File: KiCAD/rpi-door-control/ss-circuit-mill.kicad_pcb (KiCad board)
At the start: 2 copper layers, 103.5 x 49.5 mm, 26 parts, among them IC1 4N35, J1 RJ45, P1 CONN_13X2, P2 CONN_2, P3 CONN_2, P4 CONN_2, Q1 2N3904, Q2 2N3904, SW1 SW_PUSH, U1 RELAY

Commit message: 12V circuit is done but man the data side is tricky
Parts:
- P2: value CONN_2 -> LOCK BTN
- P3: value CONN_2 -> MAGLOCK
- P4: value CONN_2 -> +12V
- moved D4 67.1 mm to (179.7, 69.5)
- moved P1 57.4 mm to (96.2, 103.7), turned to 270 degrees
- moved SW1 48.1 mm to (100.2, 72.5), turned to 180 degrees
- moved J1 37.5 mm to (128.1, 70.3), turned to 180 degrees
- moved P2 34.0 mm to (112.0, 73.7), turned to 0 degrees
- moved U1 31.6 mm to (156.2, 85.0), turned to 90 degrees
- moved P4 24.1 mm to (178.4, 82.5)
- moved Q2 22.9 mm to (167.2, 101.2), turned to 0 degrees
- moved D5 21.7 mm to (159.5, 100.1), turned to 90 degrees
- moved R6 21.7 mm to (132.6, 104.5), turned to 90 degrees
- moved R12 19.2 mm to (168.3, 78.7)
- moved R1 18.9 mm to (102.2, 83.4), turned to 180 degrees
- moved P3 18.9 mm to (178.5, 100.5)
- moved R7 9.47 mm to (152.8, 99.5), turned to 270 degrees
- moved R11 6.38 mm to (136.9, 89.8)
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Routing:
- net /BELL: track 0.00 -> 67.2 mm
- net +5V: track 0.00 -> 59.6 mm
- net +12V: track 0.00 -> 54.8 mm
- net /GPIO17: track 0.00 -> 49.3 mm
- net GNDPWR: track 0.00 -> 48.7 mm
- net N-0000037: track 0.00 -> 45.8 mm
- net N-0000021: track 0.00 -> 28.3 mm
- net N-0000026: track 0.00 -> 27.9 mm
- net N-0000022: track 0.00 -> 13.0 mm
- net N-000006: track 0.00 -> 9.85 mm
- net +3.3V: track 0.00 -> 5.42 mm
- added copper zone on B.Cu, net (none)
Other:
- board size 103.5 x 49.5 mm -> 133.5 x 88.5 mm
- net class 12V POWER: clearance 2 -> 0.5; trace_width 3 -> 2
- net class Default: clearance 1 -> 0.5
- rule trace_clearance: 1 -> 0.5

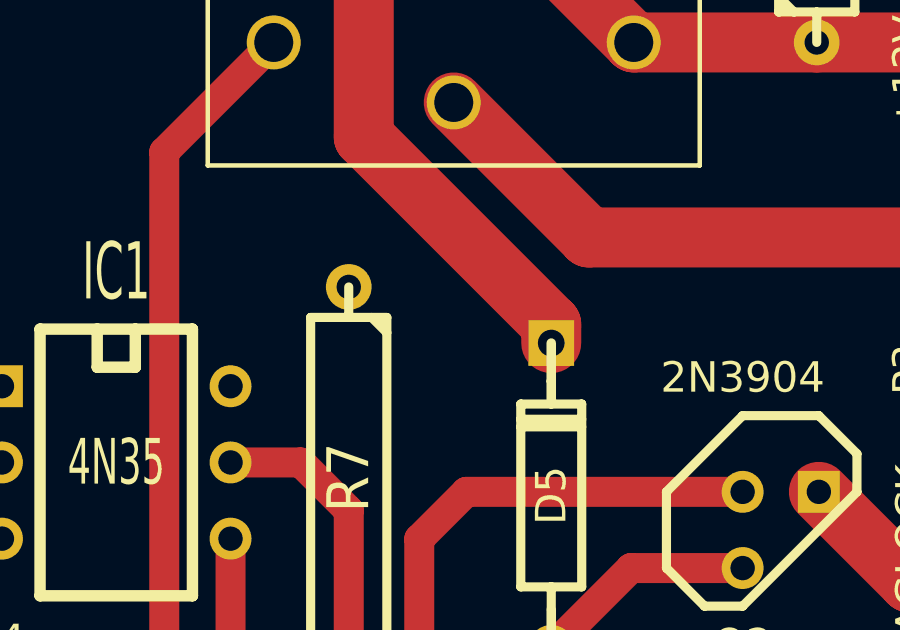
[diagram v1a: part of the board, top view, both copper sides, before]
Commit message: Missed a track on the power side
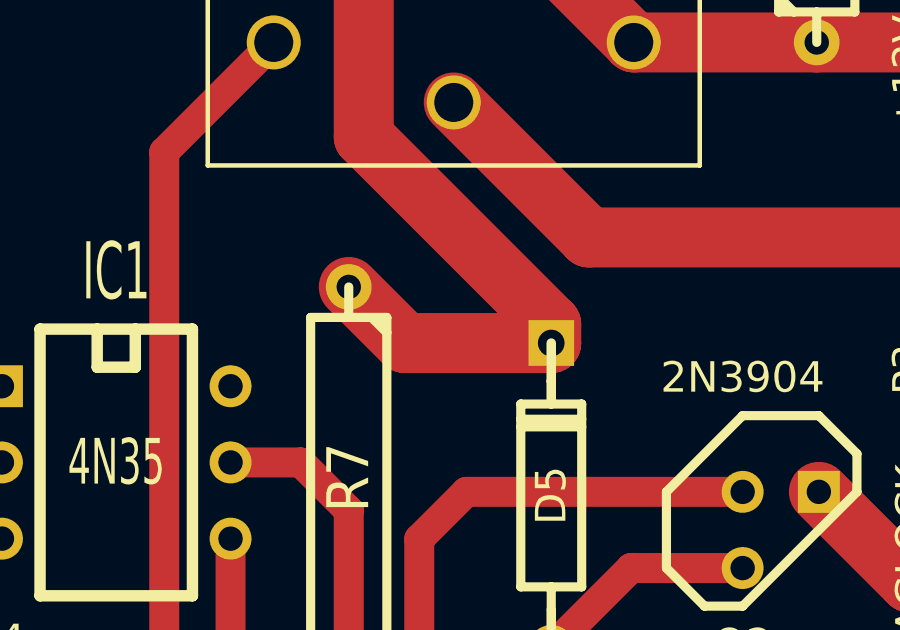
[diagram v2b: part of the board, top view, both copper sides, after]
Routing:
- net +12V: track 54.8 -> 62.3 mm
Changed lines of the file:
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@@
   (general
     (links 48)
-    (no_connects 26)
-    (area 0 0 0 0)
+    (no_connects 25)
+    (area 71.424999 52.924999 205.075001 141.575001)
     (thickness 1.6)
     (drawings 4)
-    (tracks 67)
+    (tracks 69)
     (zones 0)
     (modules 26)
@@
   (gr_line (start 205 53) (end 205 141.5) (angle 90) (layer Edge.Cuts) (width 0.15))
   (gr_line (start 71.5 53) (end 205 53) (angle 90) (layer Edge.Cuts) (width 0.15))
+  (segment (start 159.5 95.02) (end 154.62 95.02) (width 2) (layer F.Cu) (net 1) (status 400000))
+  (segment (start 154.62 95.02) (end 152.75 93.15) (width 2) (layer F.Cu) (net 1) (status 800000))
   (segment (start 159.5 95.02) (end 159.5 94.4) (width 2) (layer F.Cu) (net 1))
   (segment (start 153.25 76.5) (end 153.5 76.25) (width 2) (layer F.Cu) (net 1))
@@
   (segment (start 150.25 73) (end 153.5 76.25) (width 2) (layer F.Cu) (net 1))
   (segment (start 153.5 76.25) (end 162.25 85) (width 2) (layer F.Cu) (net 1))
-  (segment (start 94.93 88.46) (end 94.93 84.27) (width 1) (layer F.Cu) (net 2) (status 400000))
-  (segment (start 94.93 84.27) (end 95.8 83.4) (width 1) (layer F.Cu) (net 2) (status 800000))
-  (segment (start 136.9 83.45) (end 136.9 76.95) (width 1) (layer F.Cu) (net 3) (status 400000))
-  (segment (start 129.865 74.25) (end 127.465 76.65) (width 1) (layer F.Cu) (net 3) (status 800000))
+  (segment (start 94.93 88.46) (end 94.93 84.27) (width 1) (layer F.Cu) (net 2))
+  (segment (start 94.93 84.27) (end 95.8 83.4) (width 1) (layer F.Cu) (net 2))
+  (segment (start 136.9 83.45) (end 136.9 76.95) (width 1) (layer F.Cu) (net 3))
+  (segment (start 129.865 74.25) (end 127.465 76.65) (width 1) (layer F.Cu) (net 3))
   (segment (start 134.2 74.25) (end 129.865 74.25) (width 1) (layer F.Cu) (net 3))
   (segment (start 136.9 76.95) (end 134.2 74.25) (width 1) (layer F.Cu) (net 3))
-  (segment (start 97.47 88.46) (end 106.94 88.46) (width 1) (layer F.Cu) (net 3) (status 400000))
-  (segment (start 111.95 83.45) (end 136.9 83.45) (width 1) (layer F.Cu) (net 3) (status 800000))
+  (segment (start 97.47 88.46) (end 106.94 88.46) (width 1) (layer F.Cu) (net 3))
+  (segment (start 111.95 83.45) (end 136.9 83.45) (width 1) (layer F.Cu) (net 3))
   (segment (start 106.94 88.46) (end 111.95 83.45) (width 1) (layer F.Cu) (net 3))
-  (segment (start 94.93 103.7) (end 94.4 103.7) (width 1) (layer F.Cu) (net 4) (status C00000))
-  (segment (start 120.55 76.65) (end 124.925 76.65) (width 1) (layer F.Cu) (net 4) (status 800000))
+  (segment (start 94.93 103.7) (end 94.4 103.7) (width 1) (layer F.Cu) (net 4))
+  (segment (start 120.55 76.65) (end 124.925 76.65) (width 1) (layer F.Cu) (net 4))
   (segment (start 115.2 71.3) (end 120.55 76.65) (width 1) (layer F.Cu) (net 4))
   (segment (start 108.75 71.3) (end 115.2 71.3) (width 1) (layer F.Cu) (net 4))
@@
   (segment (start 91.05 76.75) (end 95.15 72.65) (width 1) (layer F.Cu) (net 4))
   (segment (start 91.05 100.35) (end 91.05 76.75) (width 1) (layer F.Cu) (net 4))
-  (segment (start 94.4 103.7) (end 91.05 100.35) (width 1) (layer F.Cu) (net 4) (status 400000))
-  (segment (start 109.45 73.7) (end 109.45 82.45) (width 1) (layer F.Cu) (net 5) (status 400000))
-  (segment (start 109.45 82.45) (end 108.5 83.4) (width 1) (layer F.Cu) (net 5) (status 800000))
-  (segment (start 103.96 75.09) (end 103.96 78.86) (width 1) (layer F.Cu) (net 5) (status 400000))
-  (segment (start 103.96 78.86) (end 108.5 83.4) (width 1) (layer F.Cu) (net 5) (status 800000))
+  (segment (start 94.4 103.7) (end 91.05 100.35) (width 1) (layer F.Cu) (net 4))
+  (segment (start 109.45 73.7) (end 109.45 82.45) (width 1) (layer F.Cu) (net 5))
+  (segment (start 109.45 82.45) (end 108.5 83.4) (width 1) (layer F.Cu) (net 5))
+  (segment (start 103.96 75.09) (end 103.96 78.86) (width 1) (layer F.Cu) (net 5))
+  (segment (start 103.96 78.86) (end 108.5 83.4) (width 1) (layer F.Cu) (net 5))
   (segment (start 94.93 101.16) (end 94.11 101.16) (width 1) (layer F.Cu) (net 5))
   (segment (start 92.6 78.83) (end 96.34 75.09) (width 1) (layer F.Cu) (net 5))

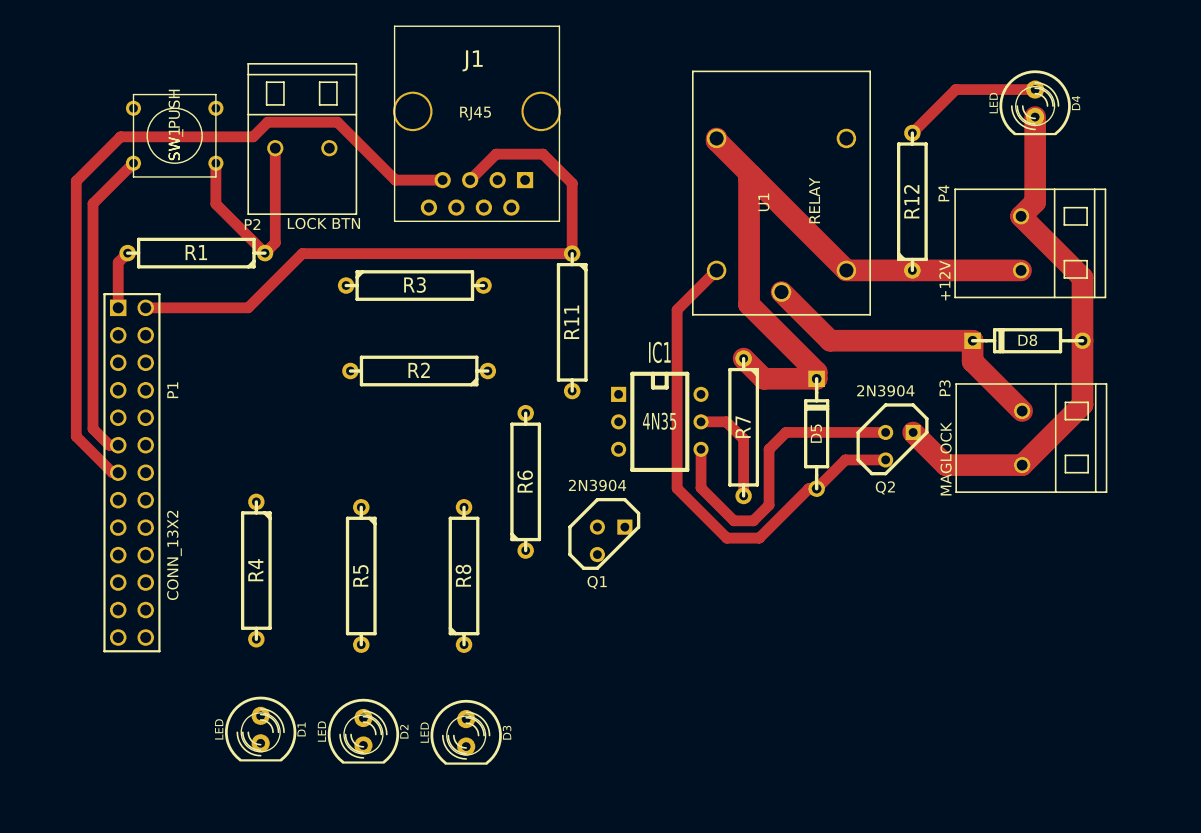
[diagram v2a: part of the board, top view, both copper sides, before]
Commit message: drew up single sided board but can't connect grounds.  Needs serious rerouting
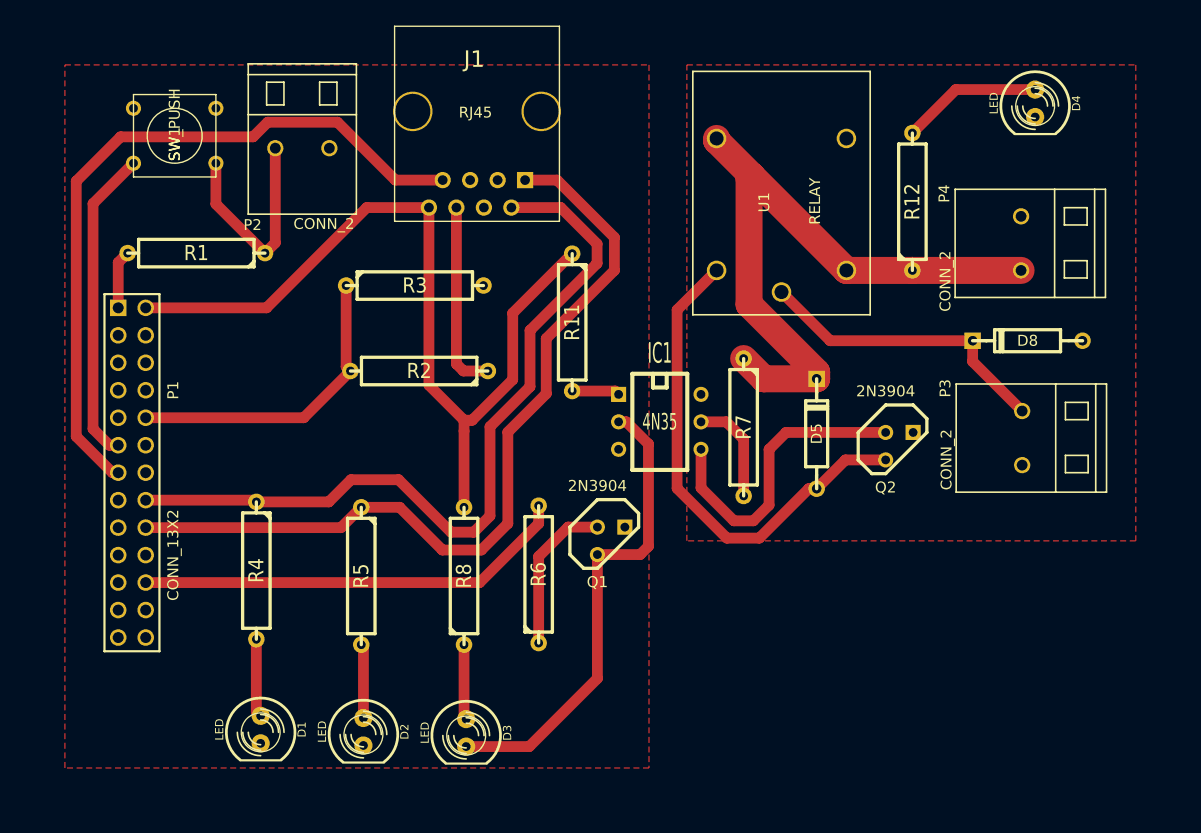
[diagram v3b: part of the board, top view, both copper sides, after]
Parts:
- P2: value LOCK BTN -> CONN_2
- P3: value MAGLOCK -> CONN_2
- P4: value +12V -> CONN_2
- moved R6 8.63 mm to (133.8, 113.1)
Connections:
- J1 pad 5: +5V -> (no net)
- J1 pad 8: (no net) -> +5V
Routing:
- net /GPIO24: track 0.00 -> 77.9 mm
- net /GPIO23: track 0.00 -> 73.9 mm
- net GNDPWR: track 48.7 -> 0.00 mm
- net N-0000025: track 0.00 -> 44.3 mm
- net /GPIO25: track 0.00 -> 40.2 mm
- net /RXD: track 0.00 -> 28.8 mm
- net +5V: track 59.6 -> 79.1 mm
- net /RFID TXD: track 0.00 -> 17.6 mm
- net N-000003: track 0.00 -> 14.6 mm
- net N-000002: track 0.00 -> 7.25 mm
- net N-0000026: track 0.00 -> 6.96 mm
- net N-000001: track 0.00 -> 6.86 mm
- net N-0000019: track 0.00 -> 4.42 mm
- added copper zone on F.Cu, net GND
- added copper zone on F.Cu, net GNDPWR
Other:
- net class 12V POWER: trace_width 2 -> 2.5

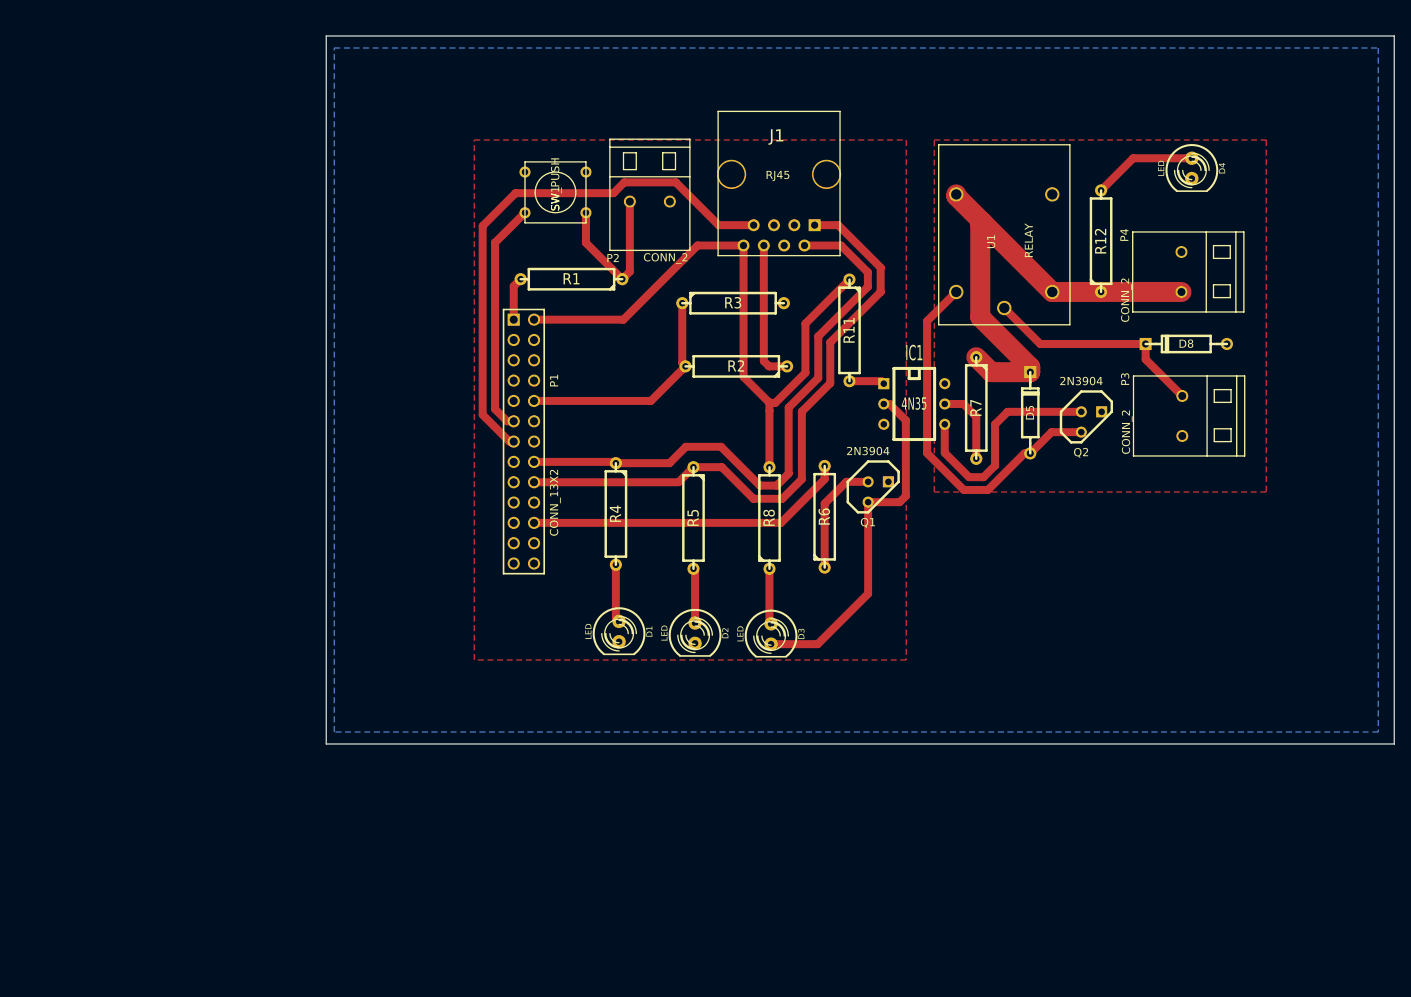
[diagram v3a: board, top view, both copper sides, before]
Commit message: Got parts traces done miraculously, just have to optimize placement now
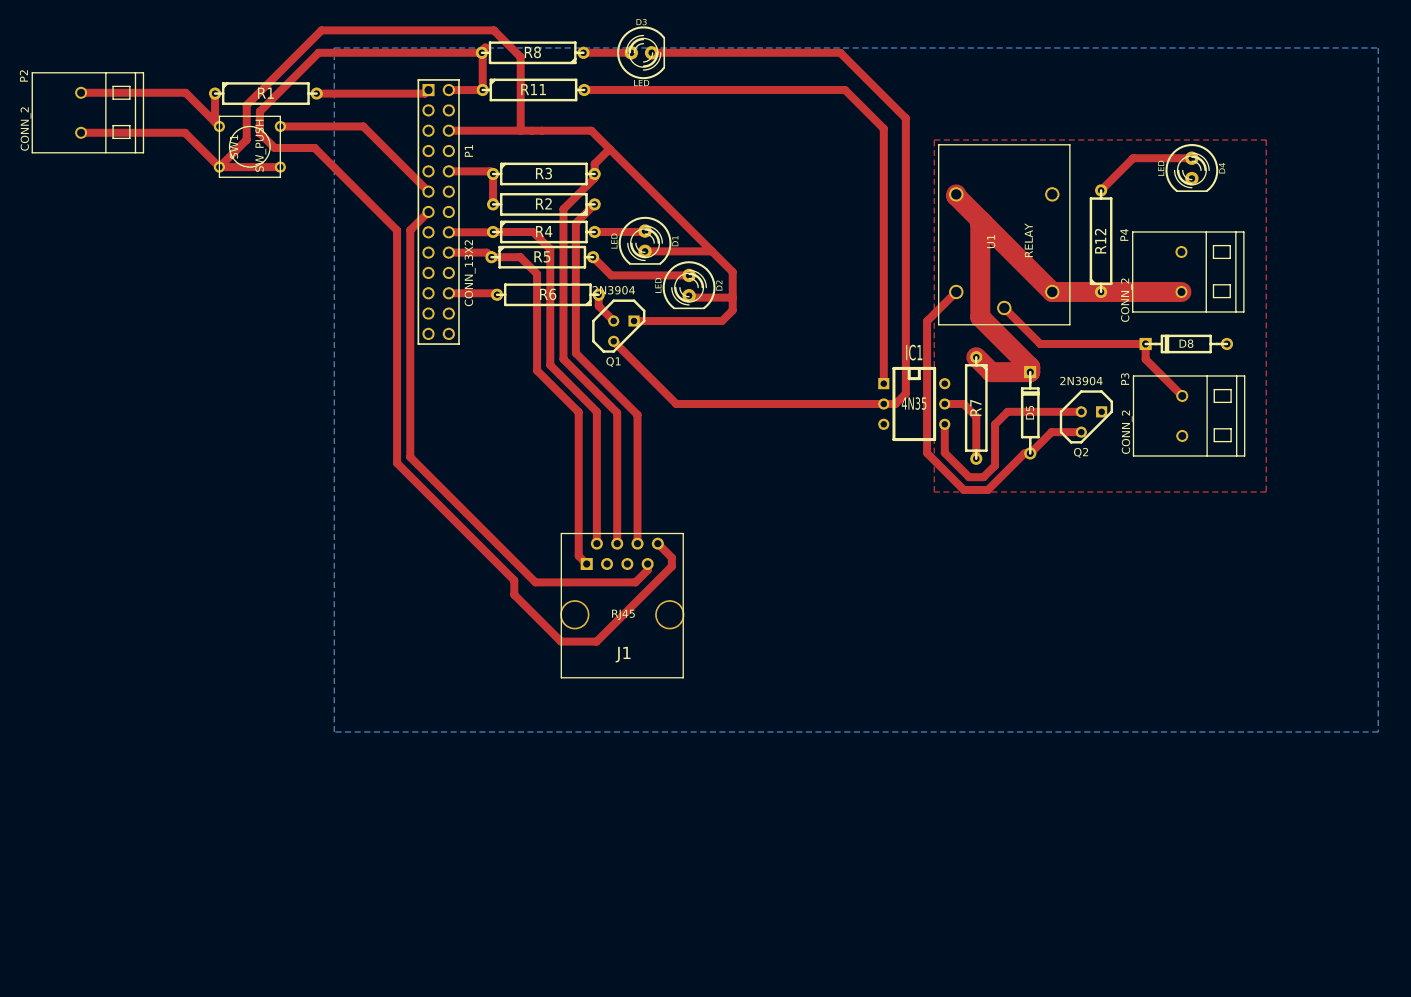
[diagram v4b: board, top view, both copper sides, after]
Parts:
- moved D3 74.4 mm to (110.9, 55.1), turned to 0 degrees
- moved P2 72.0 mm to (40.9, 62.6), turned to 270 degrees
- moved R8 65.3 mm to (97.3, 55.1), turned to 180 degrees
- moved J1 58.4 mm to (108.5, 125.3), turned to 0 degrees
- moved R11 49.6 mm to (97.4, 59.8), turned to 0 degrees
- moved D1 48.9 mm to (111.3, 78.7)
- moved R1 44.7 mm to (64.0, 60.2), turned to 0 degrees
- moved R6 44.4 mm to (99.2, 85.3), turned to 180 degrees
- moved D2 43.5 mm to (116.8, 84.2)
- moved SW1 38.6 mm to (62.0, 66.8), turned to 0 degrees
- moved R5 37.7 mm to (98.5, 80.7), turned to 0 degrees
- moved Q1 37.6 mm to (108.7, 89.9)
- moved R4 36.4 mm to (98.7, 77.5), turned to 0 degrees
- moved R2 31.4 mm to (98.7, 74.0)
- moved P1 30.6 mm to (85.5, 75.0)
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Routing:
- net GND: track 0.00 -> 213.5 mm
- net +5V: track 79.1 -> 146.6 mm
- net N-0000019: track 4.42 -> 71.3 mm
- net N-0000025: track 44.3 -> 109.9 mm
- net /GPIO25: track 40.2 -> 6.11 mm
- net /RFID TXD: track 17.6 -> 46.6 mm
- net /GPIO24: track 77.9 -> 51.0 mm
- net /GPIO23: track 73.9 -> 52.8 mm
- net /RXD: track 28.8 -> 9.47 mm
- net N-000003: track 14.6 -> 4.06 mm
- net +3.3V: track 5.42 -> 14.2 mm
- net N-000001: track 6.86 -> 12.9 mm
- net /GPIO17: track 49.3 -> 45.3 mm
- net /BELL: track 67.2 -> 69.2 mm
- net N-0000026: track 6.96 -> 5.98 mm
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- removed copper zone on F.Cu, net GND
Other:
- board outline removed

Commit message: started optimizing
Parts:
- moved J1 57.0 mm to (57.0, 100.9), turned to 270 degrees
- moved D3 48.8 mm to (128.4, 100.7), turned to 270 degrees
- moved R8 41.7 mm to (123.5, 87.5), turned to 90 degrees
- moved R11 35.5 mm to (119.5, 87.5), turned to 270 degrees
- moved D2 28.5 mm to (99.3, 106.7), turned to 180 degrees
- moved SW1 25.1 mm to (78.9, 85.5)
- moved P2 25.1 mm to (57.8, 81.2)
- moved R1 25.1 mm to (80.9, 78.8)
- moved D1 23.4 mm to (104.8, 101.2), turned to 180 degrees
- moved R3 23.4 mm to (114.5, 87.5), turned to 270 degrees
- moved P1 23.0 mm to (108.5, 75.3), turned to 180 degrees
- moved R2 17.9 mm to (110.5, 87.5), turned to 90 degrees
- moved Q1 17.4 mm to (93.6, 98.5), turned to 270 degrees
- moved R4 12.7 mm to (106.5, 87.5), turned to 270 degrees
- moved R5 7.93 mm to (102.5, 87.5), turned to 270 degrees
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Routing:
- net (no net): track 0.00 -> 927.3 mm
- net GND: track 213.5 -> 0.00 mm
- net +5V: track 146.6 -> 10.9 mm
- net N-0000025: track 109.9 -> 14.0 mm
- net N-0000019: track 71.3 -> 0.00 mm
- net /BELL: track 69.2 -> 0.00 mm
- net /GPIO23: track 52.8 -> 4.75 mm
- net /RFID TXD: track 46.6 -> 0.00 mm
- net /GPIO24: track 51.0 -> 4.91 mm
- net /GPIO17: track 45.3 -> 0.00 mm
- net +3.3V: track 14.2 -> 0.00 mm
- net N-000001: track 12.9 -> 0.00 mm
- net N-000002: track 6.35 -> 0.00 mm
- net N-000003: track 4.06 -> 0.00 mm
- net N-0000026: track 5.98 -> 7.61 mm
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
